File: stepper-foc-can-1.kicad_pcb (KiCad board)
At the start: 4 copper layers, 42 x 48 mm, 87 parts, among them J1 TC2030, J2 Conn_01x02, J3 Conn_01x04_Pin, J4 Conn_01x02, J5 Conn_01x02, M1 Stepper_Motor_bipolar, SW1 SW_Push, SW2 SW_Push, SW3 SW_Push, SW4 SW_Push, U1 STM32G474RBTx, U2 MX25947, U3 TPS62933, U4 TCAN3413, U5 AS5047P, U6 DRV8874, U7 INA241A3IDDF, U8 DRV8874, U9 INA241A3IDDF, Y1 Crystal_GND24

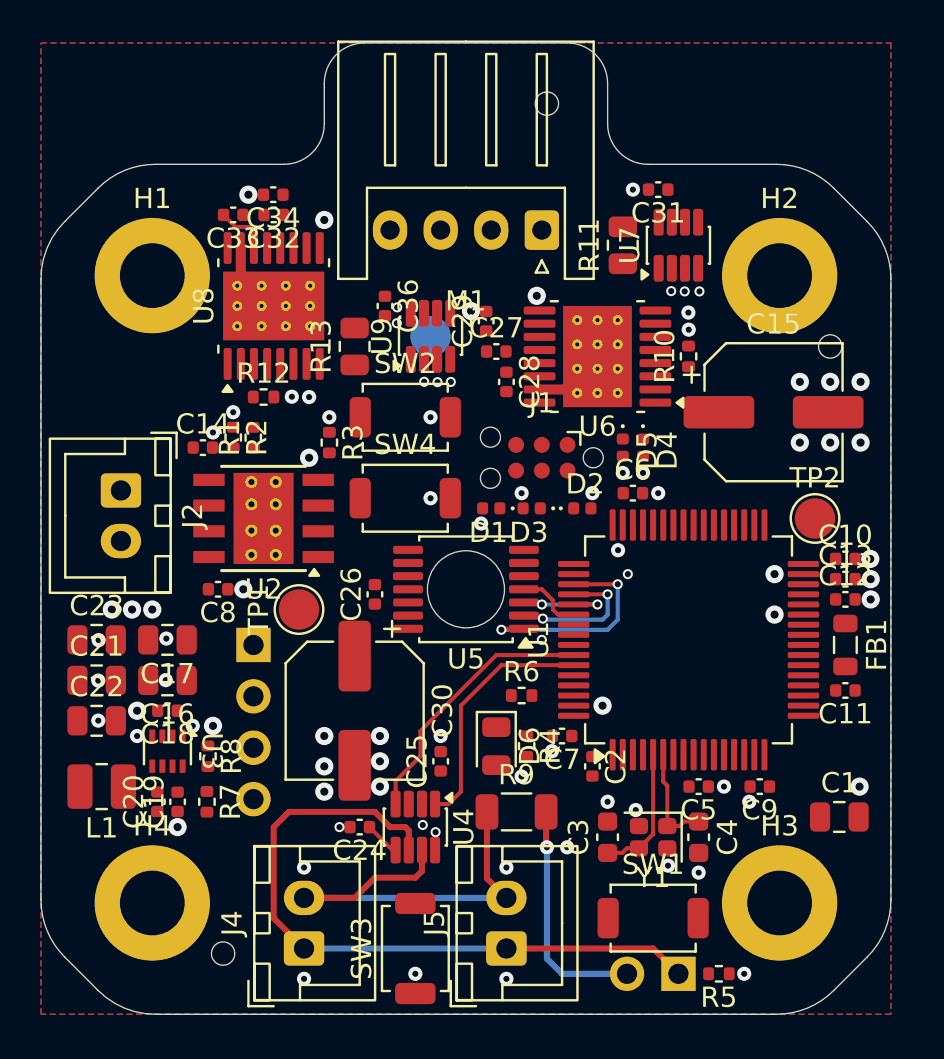
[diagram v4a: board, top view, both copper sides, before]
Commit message: pcb: add pwm routing
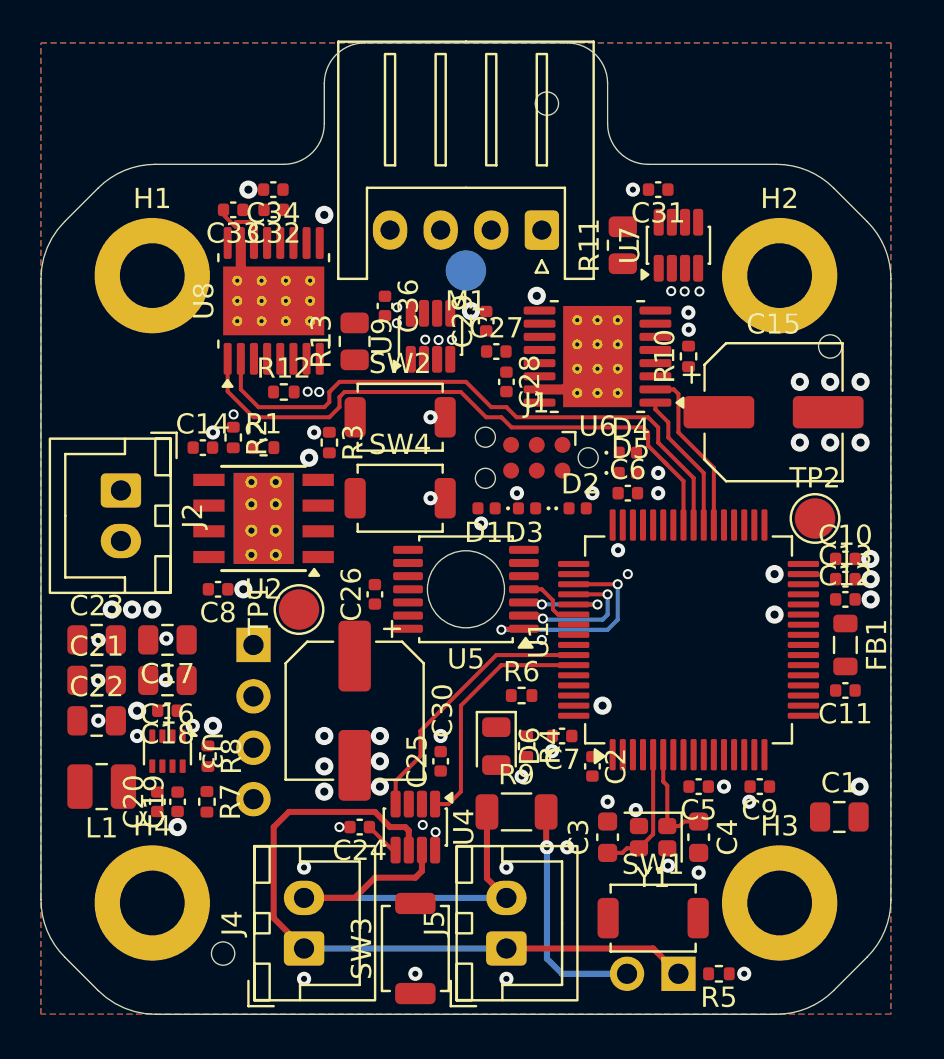
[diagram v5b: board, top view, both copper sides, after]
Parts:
- moved TP3 3.69 mm to (144.0, 65.2)
- moved D5 1.27 mm to (152.0, 75.2), turned to 0 degrees
- moved R12 1.03 mm to (135.0, 71.2)
- moved D4 0.79 mm to (152.0, 74.2), turned to 0 degrees
- moved R1 0.71 mm to (134.0, 74.0), turned to 0 degrees
- moved C32 0.25 mm to (134.5, 62.2)
- moved C33 0.25 mm to (132.5, 62.2)
- moved C34 0.25 mm to (134.5, 61.2)
- moved C6 0.25 mm to (152.0, 76.2)
- moved J1 0.25 mm to (147.5, 74.5)
- moved R13 0.25 mm to (138.5, 68.8)
- moved SW2 0.25 mm to (140.8, 72.5)
- moved SW4 0.25 mm to (140.8, 76.5)
- moved U8 0.25 mm to (134.5, 66.8)
- moved D1 0.23 mm to (145.0, 77.0)
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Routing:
- net /IN1_B: track 0.00 -> 30.1 mm
- net /IN2_B: track 0.00 -> 29.8 mm
- net /IN2_A: track 0.00 -> 8.43 mm
- net /IN1_A: track 0.00 -> 7.04 mm
- net GND: vias 84 -> 83

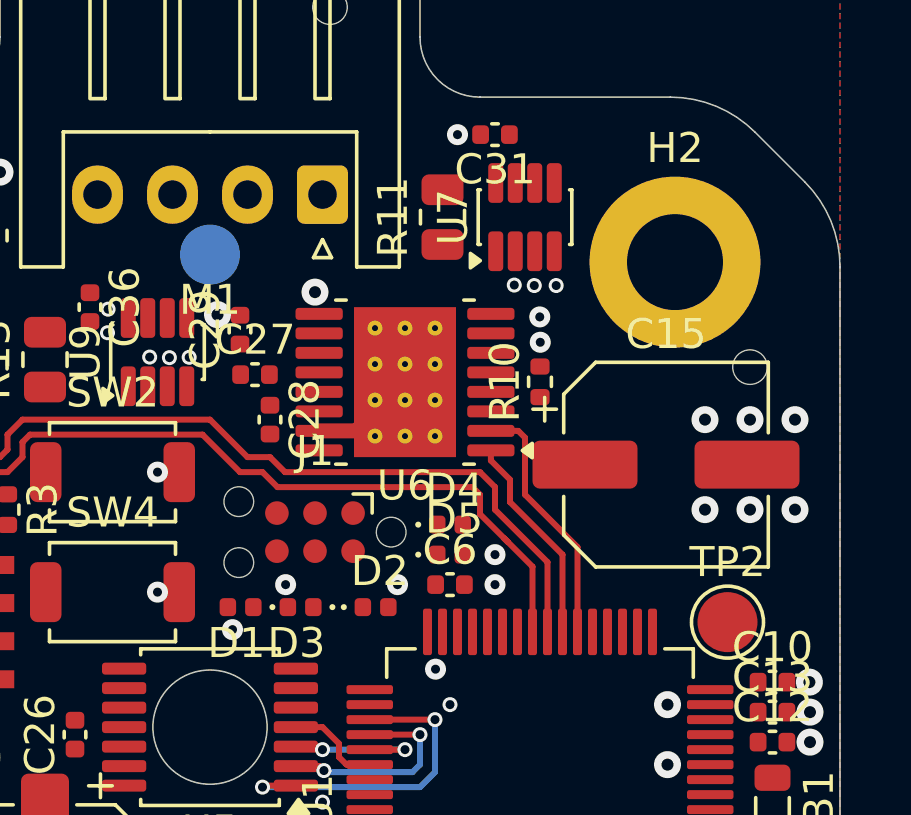
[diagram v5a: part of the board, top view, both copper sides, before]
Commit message: pcb: route analog current sense
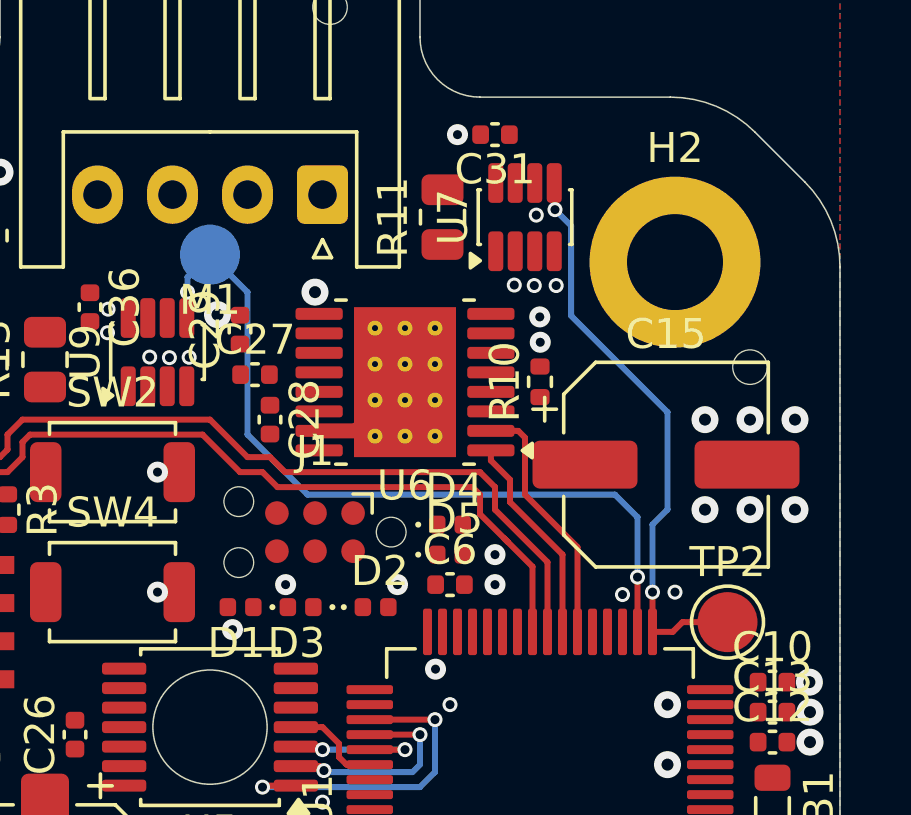
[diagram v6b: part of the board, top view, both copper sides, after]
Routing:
- net /SNS_B: track 0.00 -> 26.9 mm, vias 0 -> 2
- net /SNS_A: track 0.00 -> 19.4 mm, vias 0 -> 2
- net GND: vias 83 -> 86
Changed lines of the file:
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@@
+	)
+	(via
+		(at 157.75 76.58138)
+		(size 0.5)
+		(drill 0.3)
+		(layers "F.Cu" "B.Cu")
+		(free yes)
+		(net "GND")
 	)
 	(via
@@
 	)
 	(via
+		(at 154.876334 63.933152)
+		(size 0.5)
+		(drill 0.3)
+		(layers "F.Cu" "B.Cu")
+		(free yes)
+		(net "GND")
+	)
+	(via
 		(at 157.75 100)
 		(size 0.7)
@@
 	(via
 		(at 155.539323 66.280258)
+		(size 0.5)
+		(drill 0.3)
+		(layers "F.Cu" "B.Cu")
+		(free yes)
+		(net "GND")
+	)
+	(via
+		(at 159.5 76.5)
 		(size 0.5)
 		(drill 0.3)
@@
 	)
 	(segment
+		(start 158.75 77.825)
+		(end 158.75 76.5)
+		(width 0.2)
+		(layer "F.Cu")
+		(net "/SNS_A")
+	)
+	(segment
+		(start 159.75 77.5)
+		(end 161.25 77.5)
+		(width 0.2)
+		(layer "F.Cu")
+		(net "/SNS_A")
+	)
+	(segment
+		(start 158.75 77.825)
+		(end 159.425 77.825)
+		(width 0.2)
+		(layer "F.Cu")
+		(net "/SNS_A")
+	)
+	(segment
+		(start 159.425 77.825)
+		(end 159.75 77.5)
+		(width 0.2)
+		(layer "F.Cu")
+		(net "/SNS_A")
+	)
+	(segment
+		(start 155.5 62.8875)
+		(end 155.475 62.8625)
+		(width 0.2)
+		(layer "F.Cu")
+		(net "/SNS_A")
+	)
+	(segment
+		(start 155.5 63.75)
+		(end 155.5 62.8875)
+		(width 0.2)
+		(layer "F.Cu")
+		(net "/SNS_A")
+	)
+	(via
+		(at 155.5 63.75)
+		(size 0.5)
+		(drill 0.3)
+		(layers "F.Cu" "B.Cu")
+		(net "/SNS_A")
+	)
+	(via
+		(at 158.75 76.5)
+		(size 0.5)
+		(drill 0.3)
+		(layers "F.Cu" "B.Cu")
+		(net "/SNS_A")
+	)
+	(segment
+		(start 159.25 73.75)
+		(end 159.25 70.5)
+		(width 0.2)
+		(layer "B.Cu")
+		(net "/SNS_A")
+	)
+	(segment
+		(start 156.039323 67.289323)
+		(end 156.039323 64.289323)
+		(width 0.2)
+		(layer "B.Cu")
+		(net "/SNS_A")
+	)
+	(segment
+		(start 159.25 70.5)
+		(end 156.039323 67.289323)
+		(width 0.2)
+		(layer "B.Cu")
+		(net "/SNS_A")
+	)
+	(segment
+		(start 156.039323 64.289323)
+		(end 155.5 63.75)
+		(width 0.2)
+		(layer "B.Cu")
+		(net "/SNS_A")
+	)
+	(segment
+		(start 158.75 74.25)
+		(end 159.25 73.75)
+		(width 0.2)
+		(layer "B.Cu")
+		(net "/SNS_A")
+	)
+	(segment
+		(start 158.75 76.5)
+		(end 158.75 74.25)
+		(width 0.2)
+		(layer "B.Cu")
+		(net "/SNS_A")
+	)
+	(segment
 		(start 153.95 92.7)
 		(end 154.55 92.7)
@@
 	)
 	(segment
+		(start 143.225 67.3625)
+		(end 143.225 66.525)
+		(width 0.2)
+		(layer "F.Cu")
+		(net "/SNS_B")
+	)
+	(segment
+		(start 158.25 76)
+		(end 158.25 77.825)
+		(width 0.2)
+		(layer "F.Cu")
+		(net "/SNS_B")
+	)
+	(segment
+		(start 143.225 66.525)
+		(end 143.25 66.5)
+		(width 0.2)
+		(layer "F.Cu")
+		(net "/SNS_B")
+	)
+	(via
+		(at 143.25 66.5)
+		(size 0.5)
+		(drill 0.3)
+		(layers "F.Cu" "B.Cu")
+		(net "/SNS_B")
+	)
+	(via
+		(at 158.25 76)
+		(size 0.5)
+		(drill 0.3)
+		(layers "F.Cu" "B.Cu")
+		(net "/SNS_B")
+	)
+	(segment
+		(start 147.25 73.25)
+		(end 157.5 73.25)
+		(width 0.2)
+		(layer "B.Cu")
+		(net "/SNS_B")
+	)
+	(segment
+		(start 143.25 66)
+		(end 144 65.25)
+		(width 0.2)
+		(layer "B.Cu")
+		(net "/SNS_B")
+	)
+	(segment
+		(start 158.25 74)
+		(end 158.25 76)
+		(width 0.2)
+		(layer "B.Cu")
+		(net "/SNS_B")
+	)
+	(segment
+		(start 145.25 71.25)
+		(end 147.25 73.25)
+		(width 0.2)
+		(layer "B.Cu")
+		(net "/SNS_B")
+	)
+	(segment
+		(start 145.25 66.5)
+		(end 145.25 71.25)
+		(width 0.2)
+		(layer "B.Cu")
+		(net "/SNS_B")
+	)
+	(segment
+		(start 143.25 66.5)
+		(end 143.25 66)
+		(width 0.2)
+		(layer "B.Cu")
+		(net "/SNS_B")
+	)
+	(segment
+		(start 157.5 73.25)
+		(end 158.25 74)
+		(width 0.2)
+		(layer "B.Cu")
+		(net "/SNS_B")
+	)
+	(segment
+		(start 144 65.25)
+		(end 145.25 66.5)
+		(width 0.2)
+		(layer "B.Cu")
+		(net "/SNS_B")
+	)
+	(segment

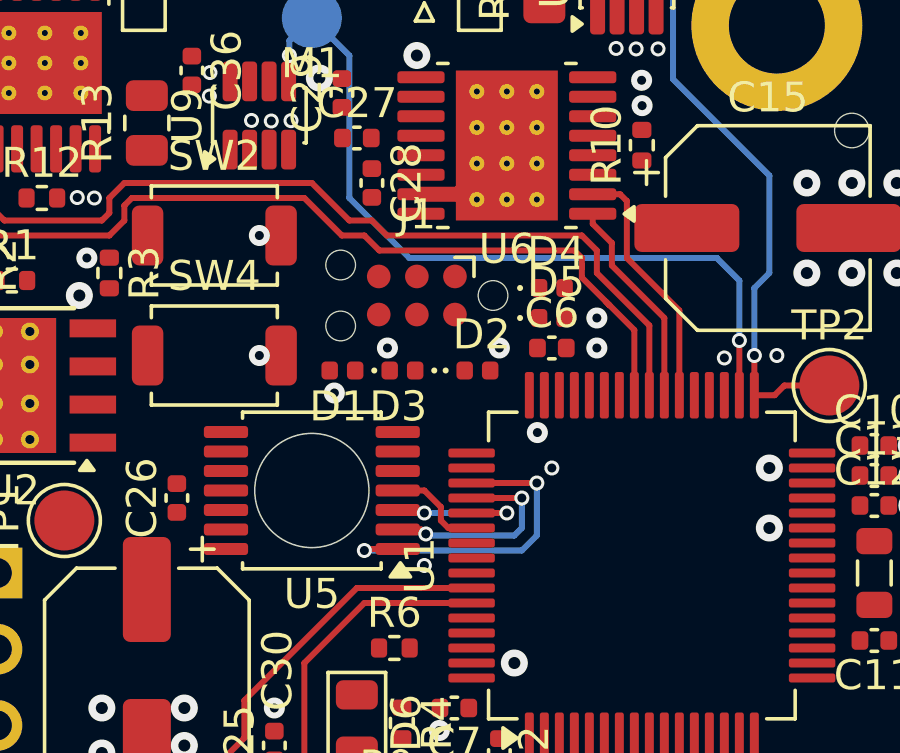
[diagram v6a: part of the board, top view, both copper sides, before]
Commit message: pcb: add swd routing
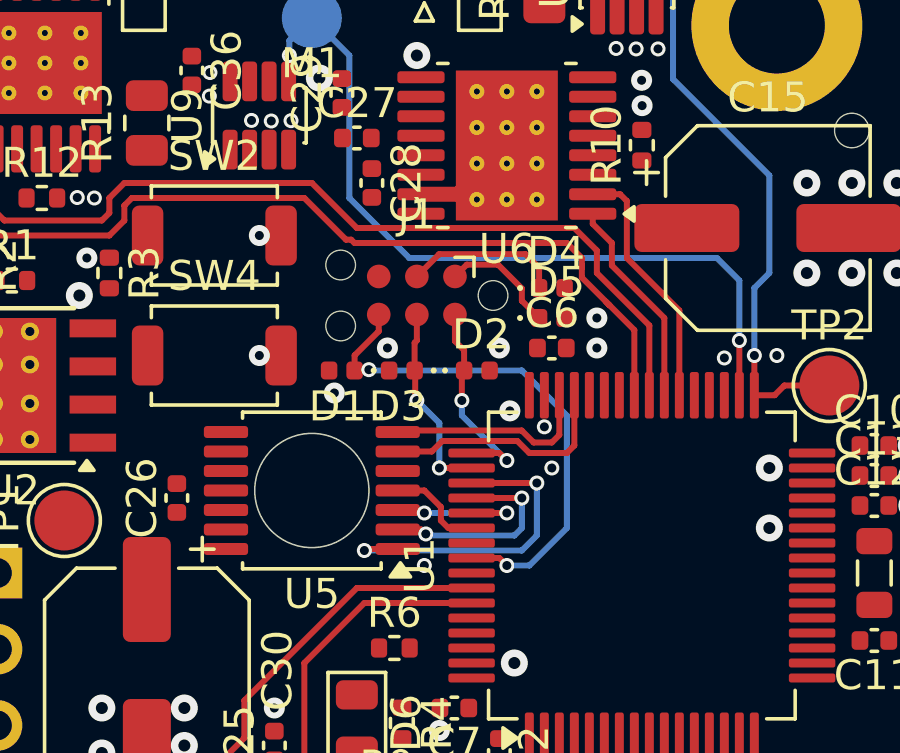
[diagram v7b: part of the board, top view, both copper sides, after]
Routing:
- net /SWO: track 0.00 -> 17.5 mm, vias 0 -> 2
- net /ENC_B: track 0.00 -> 7.98 mm
- net /ENC_A: track 0.00 -> 7.00 mm
- net /SWDIO: track 0.00 -> 6.93 mm, vias 0 -> 2
- net /SWCLK: track 0.00 -> 6.55 mm, vias 0 -> 2
- net /NRST: track 0.00 -> 5.25 mm
- net +3V3: track 1.77 -> 5.71 mm
- net GND: vias 86 -> 87
